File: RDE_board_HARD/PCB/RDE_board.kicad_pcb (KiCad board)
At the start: 2 copper layers, 160 x 100 mm, 359 parts, among them IC1 SN65HVD75DR, IC101 STPIC6C595TTR, IC102 STPIC6C595TTR, IC103 STPIC6C595TTR, IC104 STPIC6C595TTR, IC105 STPIC6C595TTR, IC106 STPIC6C595TTR, J1 DIN41612_02x32_AC, J2 TC2030, J3 Conn_01x02_Pin, J4 7772, J5 7772, J6 7772, J7 7772, K1 TQ2-5V, K10 TQ2-5V, K11 TQ2-5V, K12 TQ2-5V, K13 TQ2-5V, K14 TQ2-5V, K15 TQ2-5V, K16 TQ2-5V, K17 TQ2-5V, K18 TQ2-5V, K19 TQ2-5V, K2 TQ2-5V, K20 TQ2-5V, K21 TQ2-5V, K22 TQ2-5V, K23 TQ2-5V, K24 TQ2-5V, K25 TQ2-5V, K26 TQ2-5V, K27 TQ2-5V, K28 TQ2-5V, K29 TQ2-5V, K3 TQ2-5V, K30 TQ2-5V, K31 TQ2-5V, K32 TQ2-5V, K33 TQ2-5V, K34 TQ2-5V, K35 TQ2-5V, K36 TQ2-5V, K37 TQ2-5V, K38 TQ2-5V, K39 TQ2-5V, K4 TQ2-5V, K5 TQ2-5V, K6 TQ2-5V, K7 TQ2-5V, K8 TQ2-5V, K9 TQ2-5V, Q1 BSS138, T1 H1102NL, U1 W5500, U2 STM32G431CBTx, U3 USBLC6-2SC6, U4 USBLC6-2SC6, U5 USBLC6-2SC6, U6 FM24C64B, Y1 3225-25M-SR, Y2 3225-25M-SR

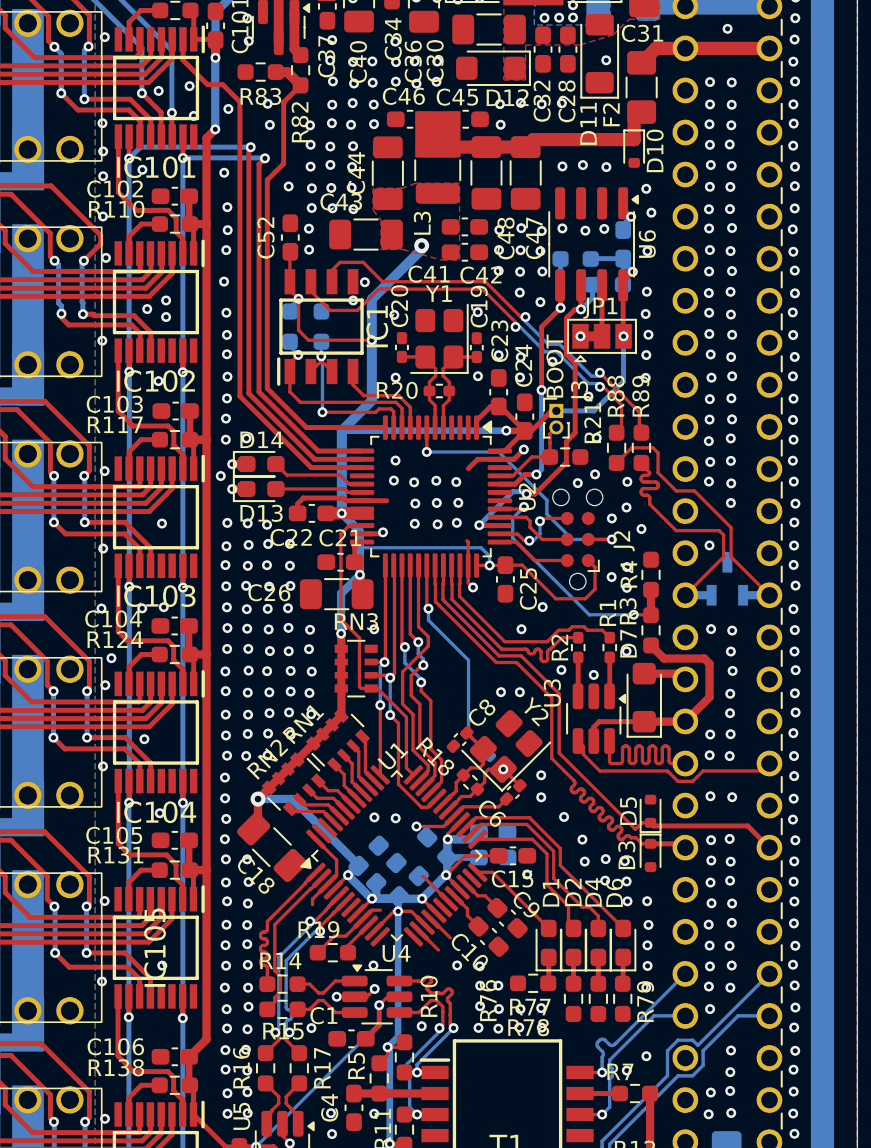
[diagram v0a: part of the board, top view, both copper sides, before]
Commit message: Added i2c for backplane config, testpoints. File organization
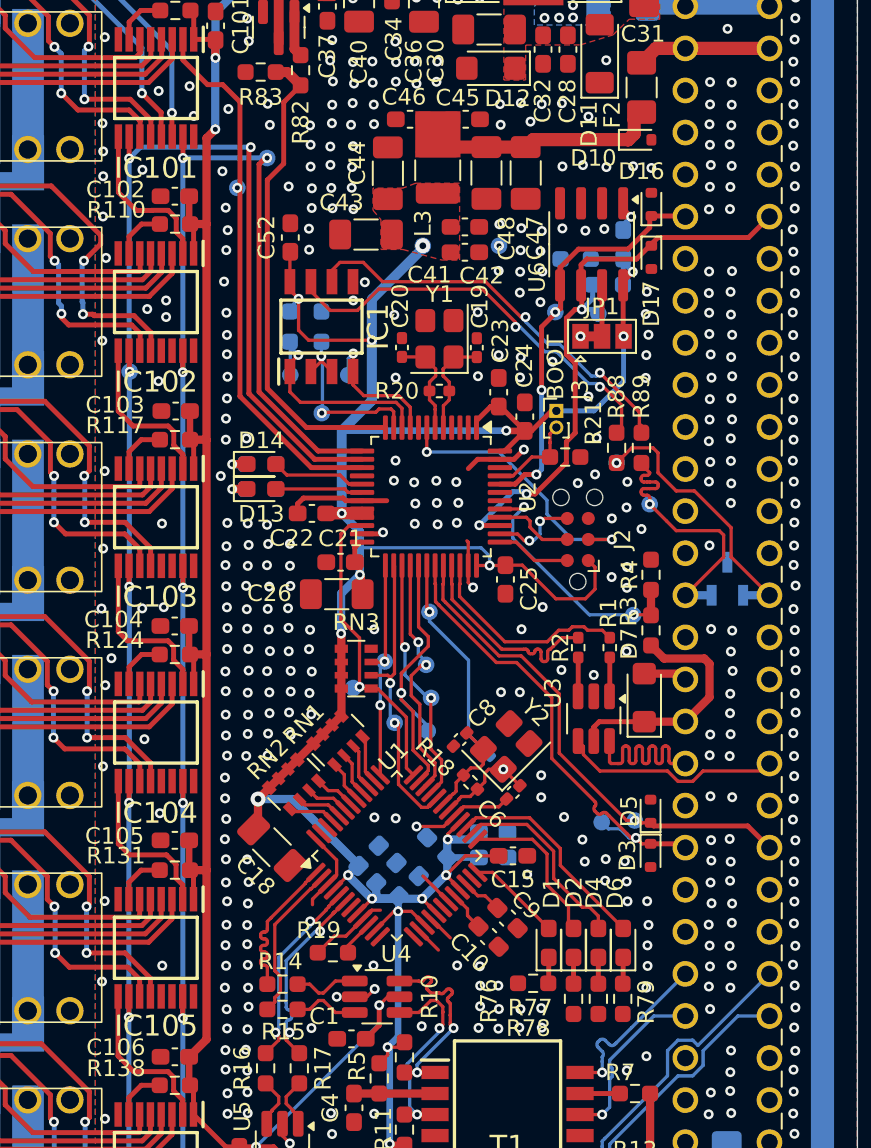
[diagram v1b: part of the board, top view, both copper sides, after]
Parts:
- added D16: ESD5Z3.3T1G, Diode_SMD:D_SOD-523, F.Cu at (217.6, 80.2)
- added D17: ESD5Z3.3T1G, Diode_SMD:D_SOD-523, F.Cu at (217.6, 83.4)
- added TP1: TestPoint, TestPoint:TestPoint_Pad_D1.0mm, B.Cu at (216.5, 105.0)
- added TP10: TestPoint, TestPoint:TestPoint_Pad_D1.0mm, B.Cu at (186.1, 90.3)
- added TP11: TestPoint, TestPoint:TestPoint_Pad_D1.0mm, B.Cu at (194.4, 77.4)
- added TP12: TestPoint, TestPoint:TestPoint_Pad_D1.0mm, B.Cu at (204.2, 104.8)
- added TP13: TestPoint, TestPoint:TestPoint_Pad_D1.0mm, B.Cu at (202.1, 111.5)
- added TP14: TestPoint, TestPoint:TestPoint_Pad_D1.0mm, B.Cu at (199.6, 109.4)
- added TP15: TestPoint, TestPoint:TestPoint_Pad_D1.0mm, B.Cu at (204.0, 108.0)
- added TP16: TestPoint, TestPoint:TestPoint_Pad_D1.0mm, B.Cu at (204.1, 112.0)
- added TP17: TestPoint, TestPoint:TestPoint_Pad_D1.0mm, B.Cu at (201.5, 107.8)
- added TP18: TestPoint, TestPoint:TestPoint_Pad_D1.0mm, B.Cu at (204.3, 110.0)
- added TP19: TestPoint, TestPoint:TestPoint_Pad_D1.0mm, B.Cu at (215.5, 95.8)
- added TP2: TestPoint, TestPoint:TestPoint_Pad_D1.0mm, B.Cu at (197.7, 92.8)
- added TP20: TestPoint, TestPoint:TestPoint_Pad_D1.0mm, B.Cu at (217.5, 98.3)
- added TP21: TestPoint, TestPoint:TestPoint_Pad_D1.0mm, B.Cu at (203.8, 82.7)
- added TP22: TestPoint, TestPoint:TestPoint_Pad_D1.0mm, B.Cu at (208.4, 82.7)
- added TP3: TestPoint, TestPoint:TestPoint_Pad_D1.0mm, B.Cu at (199.3, 90.5)
- added TP4: TestPoint, TestPoint:TestPoint_Pad_D1.0mm, B.Cu at (195.8, 90.5)
- added TP5: TestPoint, TestPoint:TestPoint_Pad_D1.0mm, B.Cu at (214.6, 117.5)
- added TP6: TestPoint, TestPoint:TestPoint_Pad_D1.0mm, B.Cu at (216.6, 117.4)
- added TP7: TestPoint, TestPoint:TestPoint_Pad_D1.0mm, B.Cu at (211.8, 86.7)
- added TP8: TestPoint, TestPoint:TestPoint_Pad_D1.0mm, B.Cu at (214.4, 86.8)
- added TP9: TestPoint, TestPoint:TestPoint_Pad_D1.0mm, B.Cu at (192.6, 79.2)
- moved D10 0.77 mm to (216.9, 76.3), turned to 0 degrees
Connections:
- J1 pad a10: unconnected-(J1-Pin_a10-Pada10) -> GND
- J1 pad a9: unconnected-(J1-Pin_a9-Pada9) -> /MCU/SCL
- J1 pad c10: unconnected-(J1-Pin_c10-Padc10) -> GND
- J1 pad c9: unconnected-(J1-Pin_c9-Padc9) -> /MCU/SDA
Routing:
- net /MCU/SCL: track 21.4 -> 37.0 mm
- net /MCU/SDA: track 17.2 -> 27.6 mm
- net /EthernetPHY/MOSI: track 14.7 -> 17.8 mm, vias 0 -> 1
- net /ConnectorDIN41612/TxD: track 6.05 -> 8.58 mm, vias 0 -> 1
- net /ConnectorDIN41612/RxD: track 11.8 -> 13.8 mm
- net /ConnectorDIN41612/USART+: track 30.3 -> 28.5 mm, vias 0 -> 1
- net /EthernetPHY/INT: track 18.4 -> 18.8 mm, vias 0 -> 1
- net /ConnectorDIN41612/USART-: track 30.4 -> 30.1 mm, vias 0 -> 1
- net /Frontend/SER_IN: track 32.7 -> 32.8 mm, vias 0 -> 1
- net GND: vias 562 -> 559
- net /ConnectorDIN41612/RS485-: vias 0 -> 1
- net /ConnectorDIN41612/RS485+: vias 0 -> 1
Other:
- board text removed: "JLCJLCJLCJLC"
